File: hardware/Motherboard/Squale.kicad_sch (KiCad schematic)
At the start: 0 parts

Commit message: WIP.
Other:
- added sheet Sound (Sound.kicad_sch)
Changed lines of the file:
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@@
+		)
+	)
+	(sheet
+		(at 50.8 92.71)
+		(size 43.18 38.1)
+		(exclude_from_sim no)
+		(in_bom yes)
+		(on_board yes)
+		(dnp no)
+		(fields_autoplaced yes)
+		(stroke
+			(width 0.1524)
+			(type solid)
+		)
+		(fill
+			(color 0 0 0 0.0000)
+		)
+		(property "Sheetname" "Sound"
+			(at 50.8 91.9984 0)
+			(effects
+				(font
+					(size 1.27 1.27)
+				)
+				(justify left bottom)
+			)
+		)
+		(property "Sheetfile" "Sound.kicad_sch"
+			(at 50.8 131.3946 0)
+			(effects
+				(font
+					(size 1.27 1.27)
+				)
+				(justify left top)
+			)
+		)
+		(instances
+			(project "Squale"
+				(path "/9e981419-a202-4dd8-b7ec-e1bde8e7b185"
+					(page "8")
+				)
+			)
 		)
 	)

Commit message: WIP
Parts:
- added U25: 74LS74, symbol 74xx:74LS74
- added U27: 74LS393, symbol 74xx:74LS393
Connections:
- new net VSS: U27.2 (MR)
- no-connect marks 0 -> 3
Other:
- title: (none) -> Apollo 7 Squale 

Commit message: WIP.
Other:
- added sheet Clocks (Clocks.kicad_sch)
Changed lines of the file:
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@@
+	)
+	(sheet
+		(at 269.24 50.8)
+		(size 12.7 3.81)
+		(exclude_from_sim no)
+		(in_bom yes)
+		(on_board yes)
+		(dnp no)
+		(fields_autoplaced yes)
+		(stroke
+			(width 0.1524)
+			(type solid)
+		)
+		(fill
+			(color 0 0 0 0.0000)
+		)
+		(property "Sheetname" "Clocks"
+			(at 269.24 50.0884 0)
+			(effects
+				(font
+					(size 1.27 1.27)
+				)
+				(justify left bottom)
+			)
+		)
+		(property "Sheetfile" "Clocks.kicad_sch"
+			(at 269.24 55.1946 0)
+			(effects
+				(font
+					(size 1.27 1.27)
+				)
+				(justify left top)
+			)
+		)
+		(instances
+			(project "Squale"
+				(path "/9e981419-a202-4dd8-b7ec-e1bde8e7b185"
+					(page "9")
+				)
+			)
+		)
 	)
 	(sheet

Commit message: WIP
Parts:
- removed U25: 74LS74, symbol 74xx:74LS74
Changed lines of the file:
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@@
-	)
-	(symbol
-		(lib_id "74xx:74LS74")
-		(at 74.93 224.79 0)
-		(unit 1)
-		(exclude_from_sim no)
-		(in_bom yes)
-		(on_board yes)
-		(dnp no)
-		(fields_autoplaced yes)
-		(property "Reference" "U25"
-			(at 77.0733 214.63 0)
-			(effects
-				(font
-					(size 1.27 1.27)
-				)
-				(justify left)
-			)
-		)
-		(property "Value" "74LS74"
-			(at 77.0733 217.17 0)
-			(effects
-				(font
-					(size 1.27 1.27)
-				)
-				(justify left)
-			)
-		)
-		(property "Footprint" ""
-			(at 74.93 224.79 0)
-			(effects
-				(font
-					(size 1.27 1.27)
-				)
-				(hide yes)
-			)
-		)
-		(property "Datasheet" "74xx/74hc_hct74.pdf"
-			(at 74.93 224.79 0)
-			(effects
-				(font
-					(size 1.27 1.27)
-				)
-				(hide yes)
-			)
-		)
-		(property "Description" "Dual D Flip-flop, Set & Reset"
-			(at 74.93 224.79 0)
-			(effects
-				(font
-					(size 1.27 1.27)
-				)
-				(hide yes)
-			)
-		)
-		(pin "13"
-		)
-		(pin "1"
-		)
-		(pin "9"
-		)
-		(pin "5"
-		)
-		(pin "6"
-		)
-		(pin "10"
-		)
-		(pin "11"
-		)
-		(pin "7"
-		)
-		(pin "3"
-		)
-		(pin "4"
-		)
-		(pin "2"
-		)
-		(pin "12"
-		)
-		(pin "8"
-		)
-		(pin "14"
-		)
-		(instances
-			(project "Squale"
-				(path "/9e981419-a202-4dd8-b7ec-e1bde8e7b185"
-					(reference "U25")
-					(unit 1)
-				)
-			)
-		)
 	)
 	(symbol

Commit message: WIP -rom pack
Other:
- removed sheet Video RAM
- added sheet System Register (sys_reg.kicad_sch)
- sheet CPU ports: added A[15..0], CLK_3.5MHz, D[7..0], EB, PA[6..0], PD[7..0], QB, R~{W}, R~{W}B, VMA, VRA, ~{CS_9365}, ~{CS_ACIA}, ~{CS_AY}, ~{CS_PIA}, ~{CS_REG}, ~{CS_V1}, ~{CS_V2}, ~{IRQ}, ~{NMI}, ~{RST}; removed none
- sheet Clocks ports: added CLK_1.75MHz, CLK_14MHz, CLK_3.5MHz, CLK_7MHz; removed none
- sheet DRAM ports: added A[15..0], D[7..0], EB, QB, R~{W}B, VMA, VRA, ~{VMA}; removed none
- sheet Keyboard ports: added EB, KEYB_CTRL, KEYB_LOCK, KEYB_SHIFT, PA[6..0], PD[7..0], ROMPACK_RST_ADDR, R~{W}B, SYSREG_KEYB_LED, ~{CS_PIA}, ~{RSTB}, ~{RST}; removed none
- sheet ROM_pack ports: added EB, PA[6..0], PD[7..0], ROMPACK_RST_ADDR, R~{W}B, ~{CS_PIA}, ~{RSTB}; removed none
- sheet Sound ports: added A0, CLK_1.75MHz, KEYB_CTRL, KEYB_LOCK, KEYB_SHIFT, LIGHTPEN_INT, MODEM_RING, PD[7..0], R~{W}B, SOUND_OUT, ~{CS_AY}, ~{RSTB}; removed none
- sheet Video Controller: file Video_CTRL.kicad_sch -> Video_RAM.kicad_sch
- sheet Video Controller ports: added CLK_1.75MHz, CLK_14MHz, CLK_3.5MHz, CLK_7MHz, COL[3..0], OpticalCK, PA[6..0], PD[7..0], R~{W}, SOUND_OUT, ~{CS_9365}, ~{CS_V1}, ~{CS_V2}, ~{IRQ}; removed none
- moved on the sheet: U27A

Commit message: wip
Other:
- added sheet Tape-Modem (tape_modem.kicad_sch)
- sheet System Register ports: added COL[3..0], PD[7..0], ~{CS_REG}, ~{RSTB}; removed none

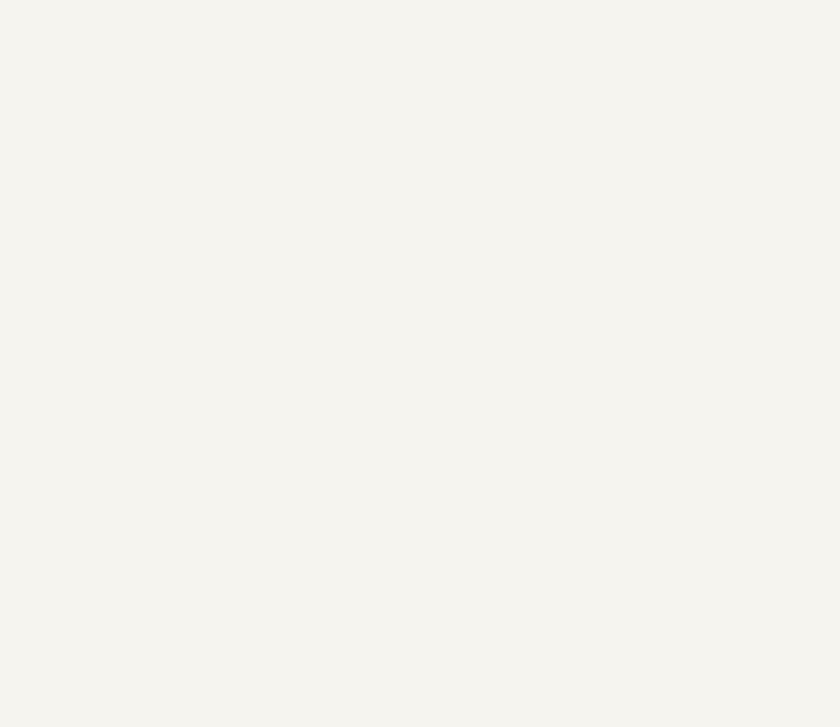
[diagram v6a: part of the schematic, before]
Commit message: S30 bus + annotations fixes.
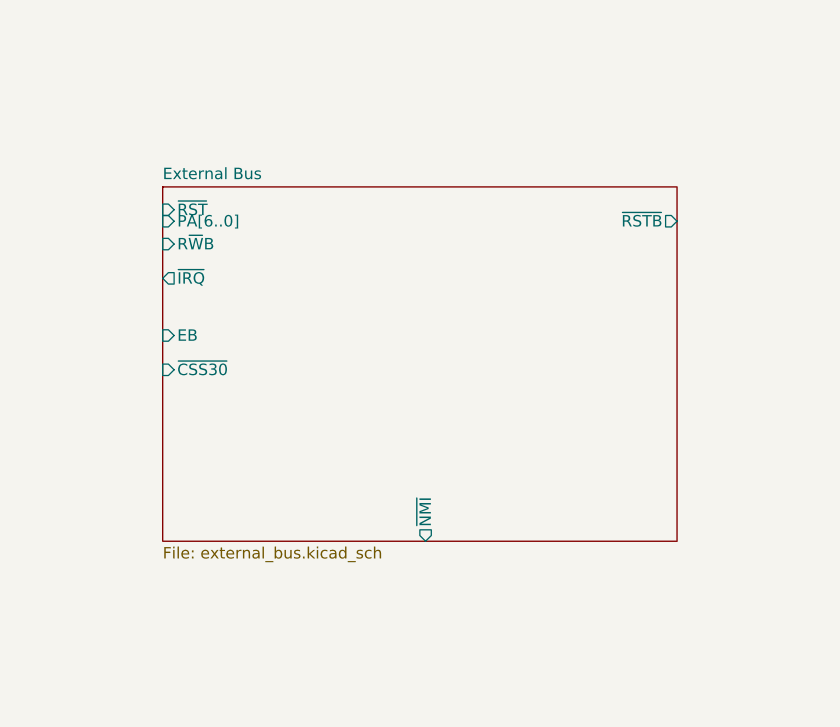
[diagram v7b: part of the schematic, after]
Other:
- added sheet External Bus (external_bus.kicad_sch)
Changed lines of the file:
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@@
+	)
+	(sheet
+		(at 96.52 201.93)
+		(size 57.15 39.37)
+		(exclude_from_sim no)
+		(in_bom yes)
+		(on_board yes)
+		(dnp no)
+		(fields_autoplaced yes)
+		(stroke
+			(width 0.1524)
+			(type solid)
+		)
+		(fill
+			(color 0 0 0 0.0000)
+		)
+		(property "Sheetname" "External Bus"
+			(at 96.52 201.2184 0)
+			(effects
+				(font
+					(size 1.27 1.27)
+				)
+				(justify left bottom)
+			)
+		)
+		(property "Sheetfile" "external_bus.kicad_sch"
+			(at 96.52 241.8846 0)
+			(effects
+				(font
+					(size 1.27 1.27)
+				)
+				(justify left top)
+			)
+		)
+		(pin "~{NMI}" output
+			(at 125.73 241.3 270)
+			(effects
+				(font
+					(size 1.27 1.27)
+				)
+				(justify left)
+			)
+		)
+		(pin "PA[6..0]" input
+			(at 96.52 205.74 180)
+			(effects
+				(font
+					(size 1.27 1.27)
+				)
+				(justify left)
+			)
+		)
+		(pin "R~{W}B" input
+			(at 96.52 208.28 180)
+			(effects
+				(font
+					(size 1.27 1.27)
+				)
+				(justify left)
+			)
+		)
+		(pin "~{RST}" input
+			(at 96.52 204.47 180)
+			(effects
+				(font
+					(size 1.27 1.27)
+				)
+				(justify left)
+			)
+		)
+		(pin "~{IRQ}" output
+			(at 96.52 212.09 180)
+			(effects
+				(font
+					(size 1.27 1.27)
+				)
+				(justify left)
+			)
+		)
+		(pin "EB" input
+			(at 96.52 218.44 180)
+			(effects
+				(font
+					(size 1.27 1.27)
+				)
+				(justify left)
+			)
+		)
+		(pin "~{CSS30}" input
+			(at 96.52 222.25 180)
+			(effects
+				(font
+					(size 1.27 1.27)
+				)
+				(justify left)
+			)
+		)
+		(pin "~{RSTB}" output
+			(at 153.67 205.74 0)
+			(effects
+				(font
+					(size 1.27 1.27)
+				)
+				(justify right)
+			)
+		)
+		(instances
+			(project "Squale"
+				(path "/9e981419-a202-4dd8-b7ec-e1bde8e7b185"
+					(page "11")
+				)
+			)
+		)
 	)
 	(sheet

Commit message: wip : modem
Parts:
- removed U27: 74LS393, symbol 74xx:74LS393
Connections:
- no-connect marks 3 -> 0
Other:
- sheet CPU ports: added ~{CSS30}; removed none
- sheet External Bus ports: added PD[7..0]; removed none
- sheet Keyboard ports: added SYS_KEYB_LED; removed SYSREG_KEYB_LED
- sheet System Register ports: added SYS_COL[3..0], SYS_KEYB_LED, SYS_MDM_LINE, SYS_MDM_MC_~{BC}, SYS_ROM_BK; removed COL[3..0]
- sheet Tape-Modem ports: added EB, PA0, PD[7..0], R~{W}B, SYS_MDM_LINE, SYS_MDM_MC_~{BC}, ~{CS_ACIA}; removed none
- sheet Video Controller ports: added SYS_COL[3..0]; removed COL[3..0]
